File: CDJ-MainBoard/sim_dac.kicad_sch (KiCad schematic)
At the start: 23 parts, among them U17 PCM5122PW

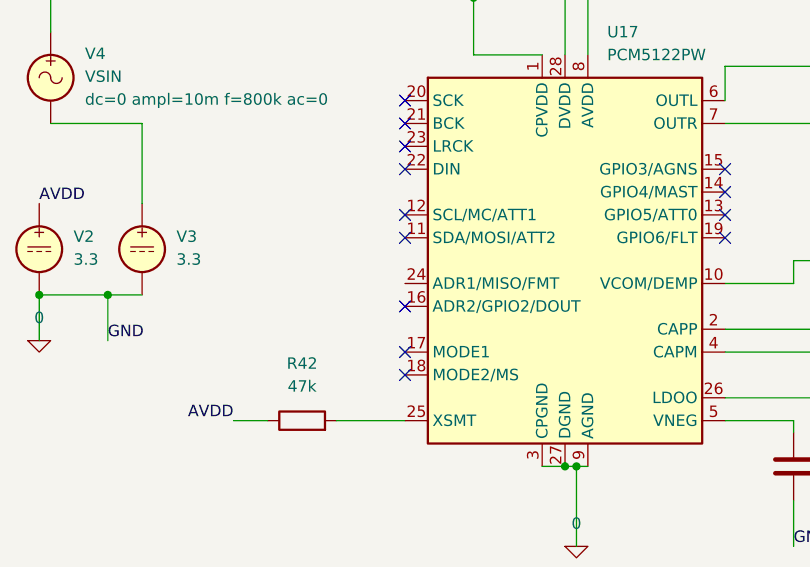
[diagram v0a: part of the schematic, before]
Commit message: Add connectors for sections of inputs, and list of all inputs in XLSX
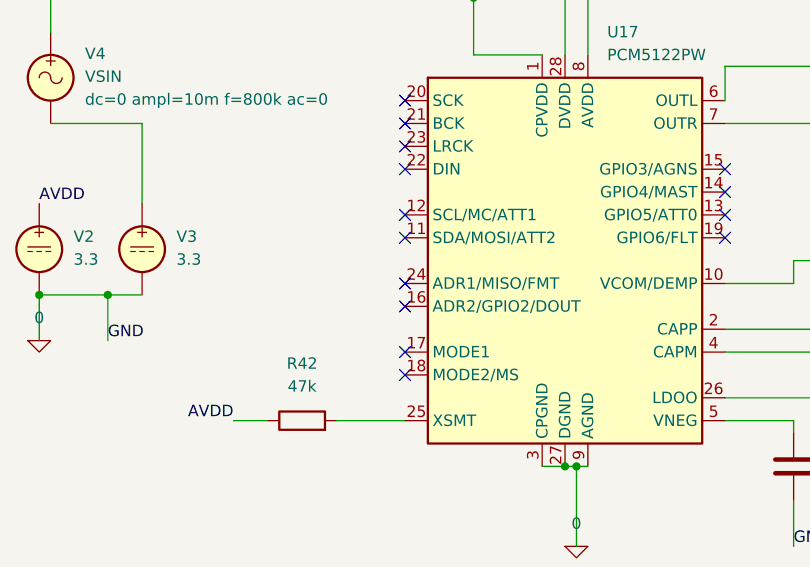
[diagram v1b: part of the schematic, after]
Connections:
- no-connect marks 13 -> 14
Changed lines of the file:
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@@
+	)
+	(no_connect
+		(at 62.23 72.39)
 	)
 	(no_connect

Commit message: Route SD card and misc
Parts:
- U17: footprint Package_SO:TSSOP-28_4.4x9.7mm_P0.65mm -> (none)
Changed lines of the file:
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@@
 			)
 		)
-		(property "Footprint" "Package_SO:TSSOP-28_4.4x9.7mm_P0.65mm"
+		(property "Footprint" ""
 			(at 80.01 69.85 0)
 			(effects
